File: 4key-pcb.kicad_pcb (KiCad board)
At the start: 2 copper layers, 80.6 x 38.2 mm, 24 parts

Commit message: started routing traces
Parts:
- moved Reset1 8.20 mm to (59.3, 117.0)
- moved R-SW1 5.19 mm to (59.4, 110.5)
- moved D4 5.06 mm to (130.9, 120.5)
- moved D1 5.06 mm to (111.9, 101.3)
- moved D3 5.00 mm to (112.0, 120.5)
- moved D2 4.89 mm to (130.8, 101.2)
- moved R-D+1 2.43 mm to (64.8, 99.5)
- moved F-USB1 1.23 mm to (57.2, 100.2)
- moved R-D-1 1.12 mm to (61.6, 99.5)
- moved USB1 0.81 mm to (63.6, 89.0)
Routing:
- net D+: track 0.00 -> 5.61 mm
- net D-: track 0.00 -> 5.61 mm
- net Net-(MCU1-Pad4): track 0.00 -> 4.93 mm
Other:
- board size 80.6 x 38.2 mm -> 82.6 x 38.1 mm
- net class Default: trace_width 0.25 -> 0.254
- net class Power added: clearance 0.2, trace_width 0.381, via_dia 0.8, via_drill 0.4

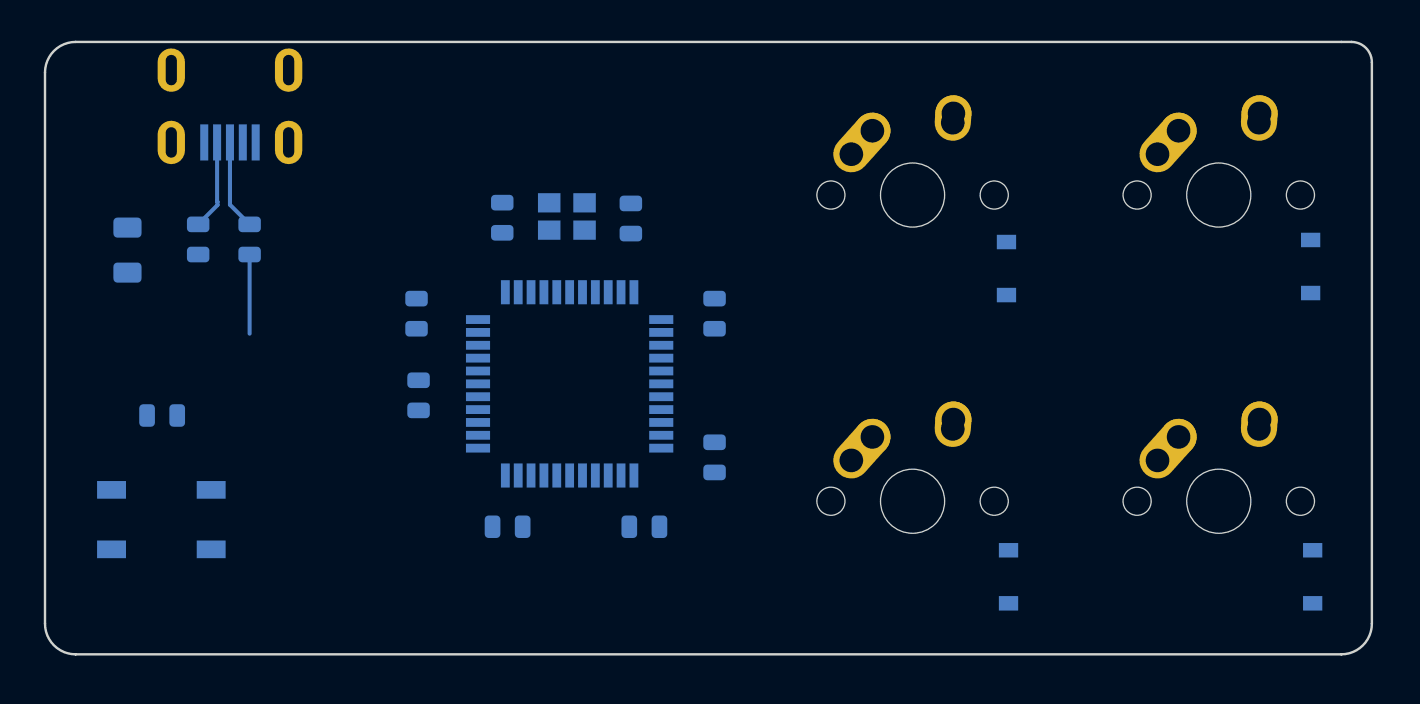
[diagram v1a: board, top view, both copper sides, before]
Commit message: finished routing mcu
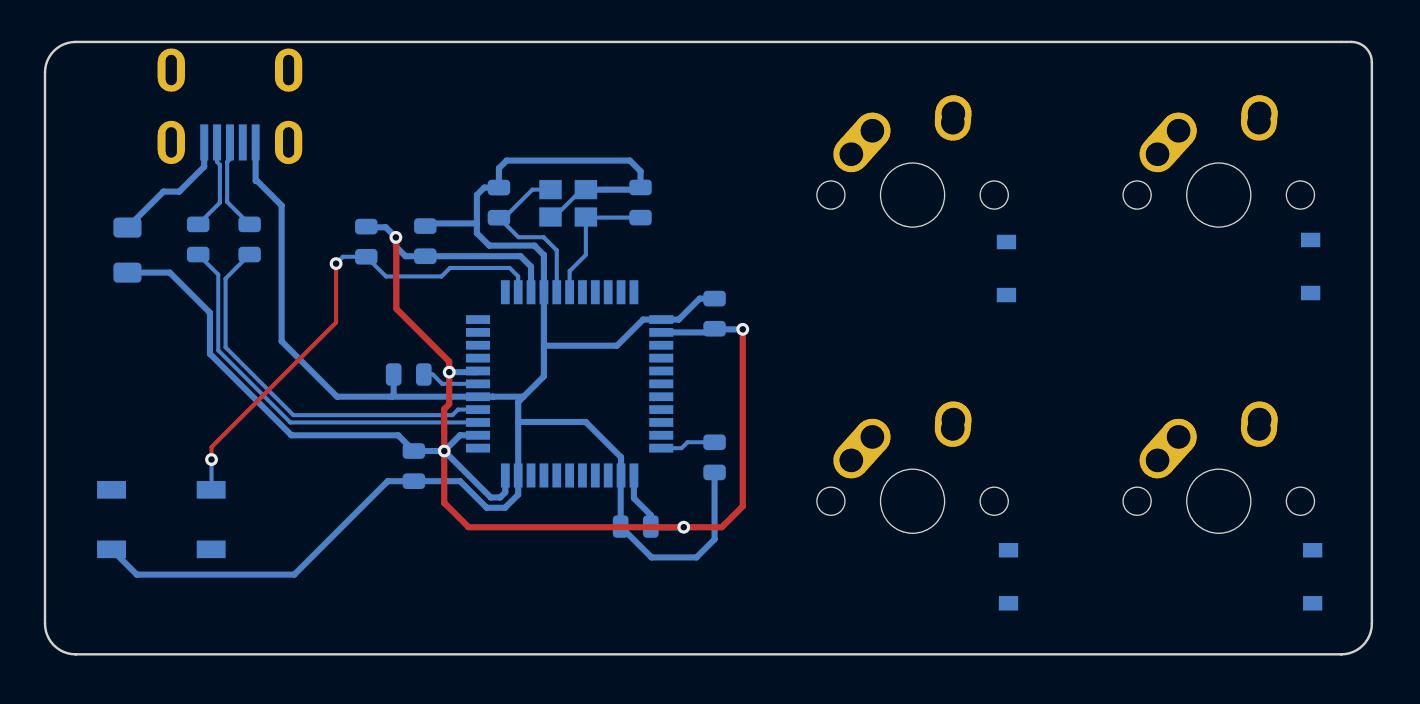
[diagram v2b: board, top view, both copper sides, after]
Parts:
- moved R-SW1 16.7 mm to (72.1, 99.7), turned to 270 degrees
- moved C4 6.95 mm to (75.0, 113.6), turned to 270 degrees
- moved C2 4.55 mm to (75.7, 99.6)
- moved C-UCAP1 1.43 mm to (74.7, 107.9), turned to 180 degrees
- moved C-C1 1.16 mm to (89.1, 97.2)
- moved C-C2 0.96 mm to (80.3, 97.2)
- moved Crytl1 0.82 mm to (84.6, 97.3), turned to 180 degrees
- moved C3 0.54 mm to (88.8, 117.4), turned to 180 degrees
- turned Reset1 to 180 degrees
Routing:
- net GND: track 0.00 -> 140.5 mm
- net +5V: track 0.00 -> 109.2 mm, vias 0 -> 5
- net Net-(MCU1-Pad13): track 0.00 -> 30.7 mm, vias 0 -> 2
- net Net-(MCU1-Pad3): track 0.00 -> 24.5 mm
- net Net-(MCU1-Pad4): track 4.93 -> 24.0 mm
- net Net-(C-C2-Pad1): track 0.00 -> 11.0 mm
- net Net-(C-C1-Pad1): track 0.00 -> 8.52 mm
- net VCC: track 0.00 -> 7.85 mm
- net Net-(MCU1-Pad33): track 0.00 -> 3.99 mm
- net Net-(C-UCAP1-Pad1): track 0.00 -> 3.63 mm

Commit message: finished pcb routing
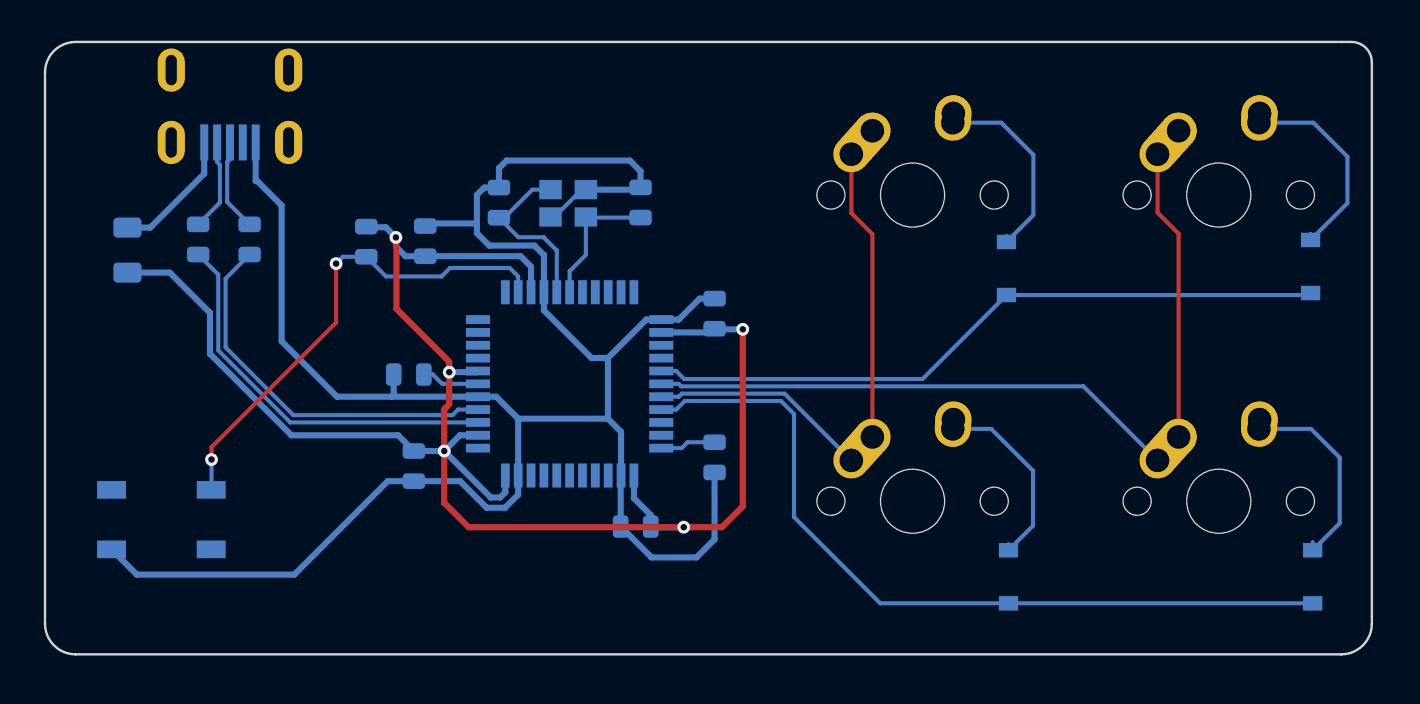
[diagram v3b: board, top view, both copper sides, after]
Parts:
- Crytl1: value Crystal -> Crystal_GND24_Small
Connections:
- MCU1 pad 27: Net-(MCU1-Pad27) -> ROW0
- MCU1 pad 28: Net-(MCU1-Pad28) -> COL1
- MCU1 pad 29: Net-(MCU1-Pad29) -> COL0
- MCU1 pad 30: Net-(MCU1-Pad30) -> ROW1
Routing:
- net COL1: track 0.00 -> 51.0 mm
- net ROW1: track 0.00 -> 49.7 mm
- net ROW0: track 0.00 -> 43.1 mm
- net COL0: track 0.00 -> 32.2 mm
- net Net-(D2-Pad2): track 0.00 -> 12.9 mm
- net Net-(D4-Pad2): track 0.00 -> 12.7 mm
- net Net-(D1-Pad2): track 0.00 -> 12.3 mm
- net Net-(D3-Pad2): track 0.00 -> 12.0 mm
- net GND: track 140.5 -> 139.6 mm

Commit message: finished pcb
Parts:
- added G***: LOGO, testboard:PCB logo - lightning bolt and B - 10mm, F.Cu at (55.7, 121.5)
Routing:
- added copper zone on B.Cu, net GND

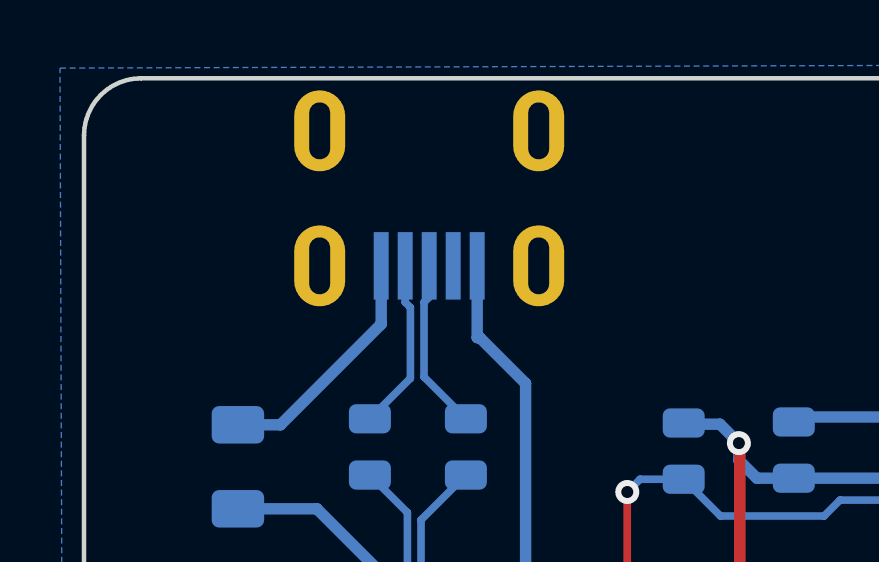
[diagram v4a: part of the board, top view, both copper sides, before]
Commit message: finally fixed footprint error
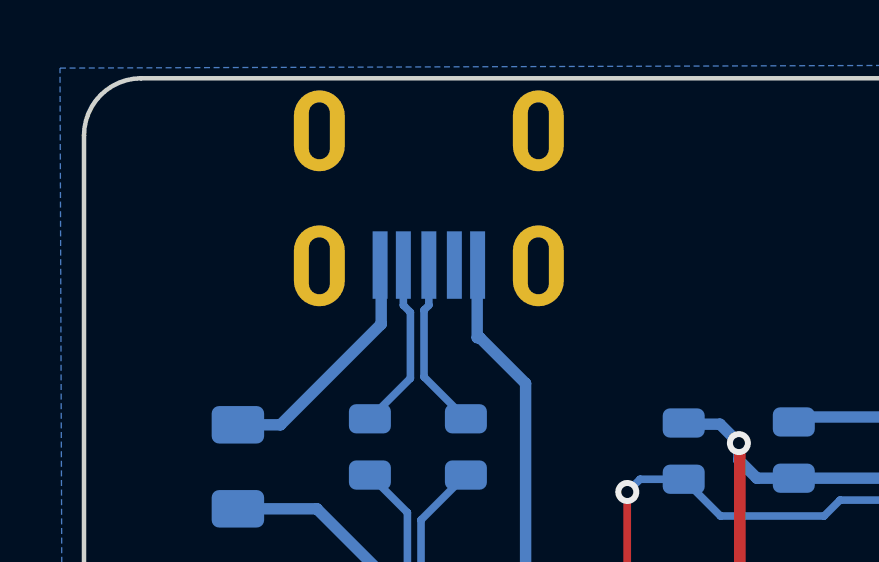
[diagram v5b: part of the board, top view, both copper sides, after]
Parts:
- moved USB1 0.92 mm to (63.6, 89.9), turned to 180 degrees
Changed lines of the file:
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@@
-(kicad_pcb (version 20171130) (host pcbnew "(5.1.8)-1")
+(kicad_pcb (version 20171130) (host pcbnew 5.1.9-73d0e3b20d~88~ubuntu16.04.1)
   (general
     (thickness 1.6)
     (drawings 9)
-    (tracks 221)
+    (tracks 222)
     (zones 0)
     (modules 25)
@@
     (add_net GND)
     (add_net VCC)
+  )
+  (module random-keyboard-parts:Molex-0548190589 (layer B.Cu)
+    (at 63.56 89.92 180)
+    (attr smd)
+    (fp_text reference USB1 (at 2.032 0 -90) (layer B.SilkS)
+      (effects (font (size 1 1) (thickness 0.15)) (justify mirror))
+    )
+    (fp_text value Molex-0548190589 (at -5.08 0 -90) (layer Dwgs.User)
+      (effects (font (size 1 1) (thickness 0.15)))
+    )
+    (fp_text user %R (at 2 0 -90) (layer B.CrtYd)
+      (effects (font (size 1 1) (thickness 0.15)) (justify mirror))
+    )
+    (fp_line (start -2.005 -4.555) (end -2.005 -2.33) (layer B.Fab) (width 0.15))
+    (fp_line (start -1.255 -4.555) (end -1.255 -2.33) (layer B.Fab) (width 0.15))
+    (fp_line (start -0.455 -4.555) (end -0.455 -2.33) (layer B.Fab) (width 0.15))
+    (fp_line (start 0.445 -4.555) (end 0.445 -2.33) (layer B.Fab) (width 0.15))
+    (fp_line (start 1.245 -4.555) (end 1.245 -2.33) (layer B.Fab) (width 0.15))
+    (fp_line (start 1.995 -4.555) (end -2.005 -4.555) (layer B.Fab) (width 0.15))
+    (fp_line (start 1.995 -4.555) (end 1.995 -2.33) (layer B.Fab) (width 0.15))
+    (fp_line (start 1.995 -2.33) (end -2.005 -2.33) (layer B.Fab) (width 0.15))
+    (fp_line (start 3.845 4.67) (end -3.855 4.67) (layer Dwgs.User) (width 0.15))
+    (fp_line (start 4.567 2.67) (end -4.577 2.67) (layer Dwgs.User) (width 0.15))
+    (fp_line (start -3.855 4.67) (end -3.855 0.92) (layer Dwgs.User) (width 0.15))
+    (fp_line (start 3.845 4.67) (end 3.845 0.92) (layer Dwgs.User) (width 0.15))
+    (fp_line (start 3.845 -4.53) (end -3.855 -4.53) (layer B.SilkS) (width 0.15))
+    (fp_line (start -3.855 0.92) (end -3.855 -4.53) (layer B.SilkS) (width 0.15))
+    (fp_line (start 3.845 0.92) (end 3.845 -4.53) (layer B.SilkS) (width 0.15))
+    (fp_line (start 3.745 4.67) (end 3.745 -4.58) (layer B.CrtYd) (width 0.05))
+    (fp_line (start 3.745 -4.58) (end -3.755 -4.58) (layer B.CrtYd) (width 0.05))
+    (fp_line (start -3.755 -4.58) (end -3.755 4.67) (layer B.CrtYd) (width 0.05))
+    (fp_line (start -3.755 4.67) (end 3.745 4.67) (layer B.CrtYd) (width 0.05))
+    (pad 6 thru_hole oval (at 3.645 0.92 270) (size 2.7 1.7) (drill oval 1.9 0.7) (layers *.Cu *.Mask)
+      (net 7 "Net-(USB1-Pad6)"))
+    (pad 6 thru_hole oval (at -3.655 0.92 270) (size 2.7 1.7) (drill oval 1.9 0.7) (layers *.Cu *.Mask)
+      (net 7 "Net-(USB1-Pad6)"))
+    (pad 6 thru_hole oval (at -3.655 -3.58 270) (size 2.7 1.7) (drill oval 1.9 0.7) (layers *.Cu *.Mask)
+      (net 7 "Net-(USB1-Pad6)"))
+    (pad 6 thru_hole oval (at 3.645 -3.58 270) (size 2.7 1.7) (drill oval 1.9 0.7) (layers *.Cu *.Mask)
+      (net 7 "Net-(USB1-Pad6)"))
+    (pad 5 smd rect (at 1.62 -3.555 270) (size 2.25 0.5) (layers B.Cu B.Paste B.Mask)
+      (net 6 VCC))
+    (pad 4 smd rect (at 0.845 -3.555 270) (size 2.25 0.5) (layers B.Cu B.Paste B.Mask)
+      (net 5 D-))
+    (pad 3 smd rect (at -0.005 -3.555 270) (size 2.25 0.5) (layers B.Cu B.Paste B.Mask)
+      (net 4 D+))
+    (pad 2 smd rect (at -0.855 -3.555 270) (size 2.25 0.5) (layers B.Cu B.Paste B.Mask)
+      (net 3 "Net-(USB1-Pad2)"))
+    (pad 1 smd rect (at -1.63 -3.555 270) (size 2.25 0.5) (layers B.Cu B.Paste B.Mask)
+      (net 1 GND))
   )
   (module "testboard:PCB logo - lightning bolt and B - 10mm" (layer F.Cu)
@@
     )
   )
-  (module random-keyboard-parts:Molex-0548190589 (layer B.Cu)
-    (at 63.5762 89.0016 270)
-    (attr smd)
-    (fp_text reference USB1 (at 2.032 0 180) (layer B.SilkS)
-      (effects (font (size 1 1) (thickness 0.15)) (justify mirror))
-    )
-    (fp_text value Molex-0548190589 (at -5.08 0 180) (layer Dwgs.User)
-      (effects (font (size 1 1) (thickness 0.15)))
-    )
-    (fp_line (start 3.25 1.25) (end 5.5 1.25) (layer B.CrtYd) (width 0.15))
-    (fp_line (start 5.5 0.5) (end 3.25 0.5) (layer B.CrtYd) (width 0.15))
-    (fp_line (start 3.25 -0.5) (end 5.5 -0.5) (layer B.CrtYd) (width 0.15))
-    (fp_line (start 5.5 -1.25) (end 3.25 -1.25) (layer B.CrtYd) (width 0.15))
-    (fp_line (start 3.25 -2) (end 5.5 -2) (layer B.CrtYd) (width 0.15))
-    (fp_line (start 3.25 2) (end 3.25 -2) (layer B.CrtYd) (width 0.15))
-    (fp_line (start 5.5 2) (end 3.25 2) (layer B.CrtYd) (width 0.15))
-    (fp_line (start -3.75 -3.75) (end -3.75 3.75) (layer B.CrtYd) (width 0.15))
-    (fp_line (start 5.5 -3.75) (end -3.75 -3.75) (layer B.CrtYd) (width 0.15))
-    (fp_line (start 5.5 3.75) (end 5.5 -3.75) (layer B.CrtYd) (width 0.15))
-    (fp_line (start -3.75 3.75) (end 5.5 3.75) (layer B.CrtYd) (width 0.15))
-    (fp_line (start 0 3.85) (end 5.45 3.85) (layer B.SilkS) (width 0.15))
-    (fp_line (start 0 -3.85) (end 5.45 -3.85) (layer B.SilkS) (width 0.15))
-    (fp_line (start 5.45 3.85) (end 5.45 -3.85) (layer B.SilkS) (width 0.15))
-    (fp_line (start -3.75 3.85) (end 0 3.85) (layer Dwgs.User) (width 0.15))
-    (fp_line (start -3.75 -3.85) (end 0 -3.85) (layer Dwgs.User) (width 0.15))
-    (fp_line (start -1.75 4.572) (end -1.75 -4.572) (layer Dwgs.User) (width 0.15))
-    (fp_line (start -3.75 3.85) (end -3.75 -3.85) (layer Dwgs.User) (width 0.15))
-    (fp_text user %R (at 2 0 180) (layer B.CrtYd)
-      (effects (font (size 1 1) (thickness 0.15)) (justify mirror))
-    )
-    (pad 1 smd rect (at 4.5 -1.6 270) (size 2.25 0.5) (layers B.Cu B.Paste B.Mask)
-      (net 1 GND))
-    (pad 2 smd rect (at 4.5 -0.8 270) (size 2.25 0.5) (layers B.Cu B.Paste B.Mask)
-      (net 3 "Net-(USB1-Pad2)"))
-    (pad 3 smd rect (at 4.5 0 270) (size 2.25 0.5) (layers B.Cu B.Paste B.Mask)
-      (net 4 D+))
-    (pad 4 smd rect (at 4.5 0.8 270) (size 2.25 0.5) (layers B.Cu B.Paste B.Mask)
-      (net 5 D-))
-    (pad 5 smd rect (at 4.5 1.6 270) (size 2.25 0.5) (layers B.Cu B.Paste B.Mask)
-      (net 6 VCC))
-    (pad 6 thru_hole oval (at 4.5 3.65 270) (size 2.7 1.7) (drill oval 1.9 0.7) (layers *.Cu *.Mask)
-      (net 7 "Net-(USB1-Pad6)"))
-    (pad 6 thru_hole oval (at 4.5 -3.65 270) (size 2.7 1.7) (drill oval 1.9 0.7) (layers *.Cu *.Mask)
-      (net 7 "Net-(USB1-Pad6)"))
-    (pad 6 thru_hole oval (at 0 -3.65 270) (size 2.7 1.7) (drill oval 1.9 0.7) (layers *.Cu *.Mask)
-      (net 7 "Net-(USB1-Pad6)"))
-    (pad 6 thru_hole oval (at 0 3.65 270) (size 2.7 1.7) (drill oval 1.9 0.7) (layers *.Cu *.Mask)
-      (net 7 "Net-(USB1-Pad6)"))
-  )
   (module random-keyboard-parts:SKQG-1155865 (layer B.Cu)
     (at 59.309 116.967 180)
@@
   (segment (start 62.43 115.096) (end 62.409 115.117) (width 0.254) (layer B.Cu) (net 2))
   (segment (start 62.43 113.23) (end 62.43 115.096) (width 0.254) (layer B.Cu) (net 2))
-  (segment (start 63.5762 94.5438) (end 63.40401 94.71599) (width 0.254) (layer B.Cu) (net 4))
-  (segment (start 63.5762 93.5016) (end 63.5762 94.5438) (width 0.254) (layer B.Cu) (net 4))
   (segment (start 63.40401 97.20401) (end 64.8 98.6) (width 0.254) (layer B.Cu) (net 4))
-  (segment (start 63.40401 94.71599) (end 63.40401 97.20401) (width 0.254) (layer B.Cu) (net 4))
-  (segment (start 62.7762 93.5016) (end 62.7762 94.7162) (width 0.254) (layer B.Cu) (net 5))
-  (segment (start 62.7762 94.7162) (end 62.95 94.89) (width 0.254) (layer B.Cu) (net 5))
+  (segment (start 63.40401 97.20401) (end 63.40401 94.97599) (width 0.254) (layer B.Cu) (net 4))
+  (segment (start 63.565 94.815) (end 63.565 93.475) (width 0.254) (layer B.Cu) (net 4))
+  (segment (start 63.40401 94.97599) (end 63.565 94.815) (width 0.254) (layer B.Cu) (net 4))
   (segment (start 62.95 97.25) (end 61.6 98.6) (width 0.254) (layer B.Cu) (net 5))
-  (segment (start 62.95 94.89) (end 62.95 97.25) (width 0.254) (layer B.Cu) (net 5))
+  (segment (start 62.95 97.25) (end 62.95 95.05) (width 0.254) (layer B.Cu) (net 5))
+  (segment (start 62.715 94.815) (end 62.715 93.475) (width 0.254) (layer B.Cu) (net 5))
+  (segment (start 62.95 95.05) (end 62.715 94.815) (width 0.254) (layer B.Cu) (net 5))
   (segment (start 57.2 98.8) (end 58.62 98.8) (width 0.381) (layer B.Cu) (net 6))
-  (segment (start 61.9762 95.4438) (end 61.9762 93.5016) (width 0.381) (layer B.Cu) (net 6))
   (segment (start 58.62 98.8) (end 61.9762 95.4438) (width 0.381) (layer B.Cu) (net 6))
+  (segment (start 61.9762 93.5112) (end 61.94 93.475) (width 0.381) (layer B.Cu) (net 6))
+  (segment (start 61.9762 95.4438) (end 61.9762 93.5112) (width 0.381) (layer B.Cu) (net 6))
   (segment (start 57.2 101.6) (end 57.2 101.61) (width 0.381) (layer B.Cu) (net 8))
   (segment (start 57.2 101.6) (end 59.83249 101.6) (width 0.381) (layer B.Cu) (net 8))
